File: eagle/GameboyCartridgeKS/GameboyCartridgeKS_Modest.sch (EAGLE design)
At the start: 20 parts, among them IC2 MEGA64-A, Y1 16MHz max

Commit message: Modest beta before wiring
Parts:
- added JOE: JUMPER-PAD-3-NOYES_SILK, SparkFun-Passives:JUMPER-PAD-3-NOYES_SILK
- added SCL, SCL1, SCL2, SCL3, SCL4, SDA: TEST-POINT3X5, SparkFun-Passives:TEST-POINT3X5
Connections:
- removed net 10: U$1.A4
- removed net 11: U$1.A5
- removed net 12: U$1.A6
- removed net 13: U$1.A7
- removed net 14: U$1.A8
- removed net 15: U$1.A9
- removed net 16: U$1.A10
- removed net 17: U$1.A11
- removed net 18: U$1.A12
- removed net 19: U$1.A13
- removed net 20: U$1.A14
- removed net 3: U$1./WR
- removed net 30: U$1./RS
- removed net 5: U$1./RCS
- removed net 6: U$1.A0
- removed net 7: U$1.A1
- removed net 8: U$1.A2
- removed net 9: U$1.A3
- new net !GB_CS: IC2.(XCK1)PD5, SCL4.1, U$1./RCS
- new net !GB_RD: IC2.(IC1)PD4, JOE.3, SCL3.1, U$1./RD
- new net !GB_RESET: IC2.(T1)PD6, U$1./RS
- new net !GB_WR: IC2.(TXD1/INT3)PD3, SCL2.1, U$1./WR
- new net GB_CLOCK: IC2.(RXD1/INT2)PD2, SCL1.1, U$1.NC
- new net GB_MIC_IN: IC2.(OC2/OC1C)PB7, U$1.VIN
- new net N$1: IC2.(SDA/INT1)PD1, SDA.1
- new net N$5: IC2.(SCL/INT0)PD0, SCL.1
- new net N$7: IC2.(OC0)PB4, JOE.1
- net !CE: now also IC2.(MISO)PB3; no longer U$1.A15
- net !OE: now also JOE.2; no longer U$1./RD
- net !RESET: now also IC2.(OC1B)PB6
- net !WE: now also IC2.(OC1A)PB5; no longer U$1.VIN
- net ADDRESS0: now also IC2.PF0(ADC0), U$1.A0; no longer IC2.(SCL/INT0)PD0
- net ADDRESS1: now also IC2.PF1(ADC1), U$1.A1; no longer IC2.(SDA/INT1)PD1
- net ADDRESS10: now also U$1.A10
- net ADDRESS11: now also U$1.A11
- net ADDRESS12: now also U$1.A12
- net ADDRESS13: now also U$1.A13
- net ADDRESS14: now also U$1.A14
- net ADDRESS15: now also U$1.A15
- net ADDRESS2: now also IC2.PF2(ADC2), U$1.A2; no longer IC2.(RXD1/INT2)PD2
- net ADDRESS3: now also IC2.PF3(ADC3), U$1.A3; no longer IC2.(TXD1/INT3)PD3
- net ADDRESS4: now also IC2.PF4(ADC4/TCK), U$1.A4; no longer IC2.(IC1)PD4
- net ADDRESS5: now also IC2.PF5(ADC5/TMS), U$1.A5; no longer IC2.(XCK1)PD5
- net ADDRESS6: now also IC2.PF6(ADC6/TDO), U$1.A6; no longer IC2.(T1)PD6
- net ADDRESS7: now also IC2.PF7(ADC7/TDI), U$1.A7; no longer IC2.(T2)PD7
- net ADDRESS8: now also U$1.A8
- net ADDRESS9: now also U$1.A9
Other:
- moved on the sheet: D1, JD1, PEN, TP1, TP2, TP3, TP4, TP5, TP6

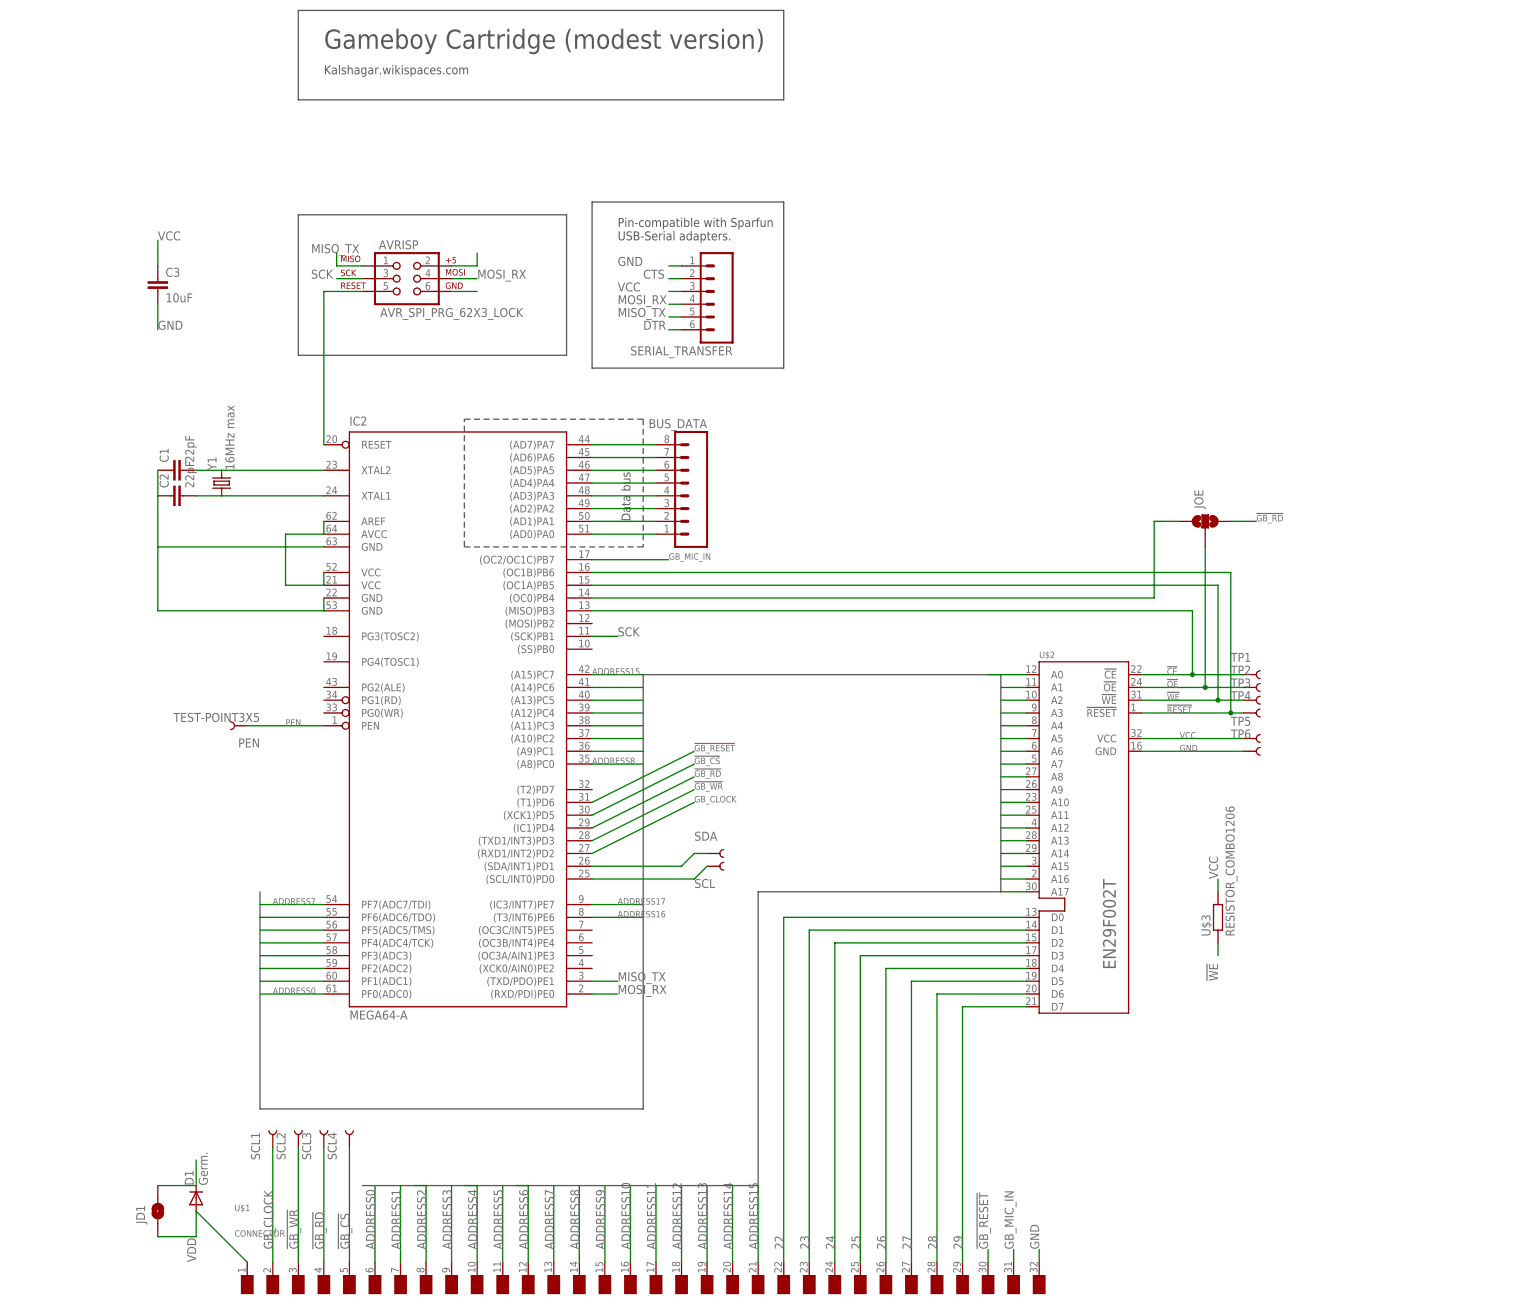
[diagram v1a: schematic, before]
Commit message: Schema finished, TODO start final placement.
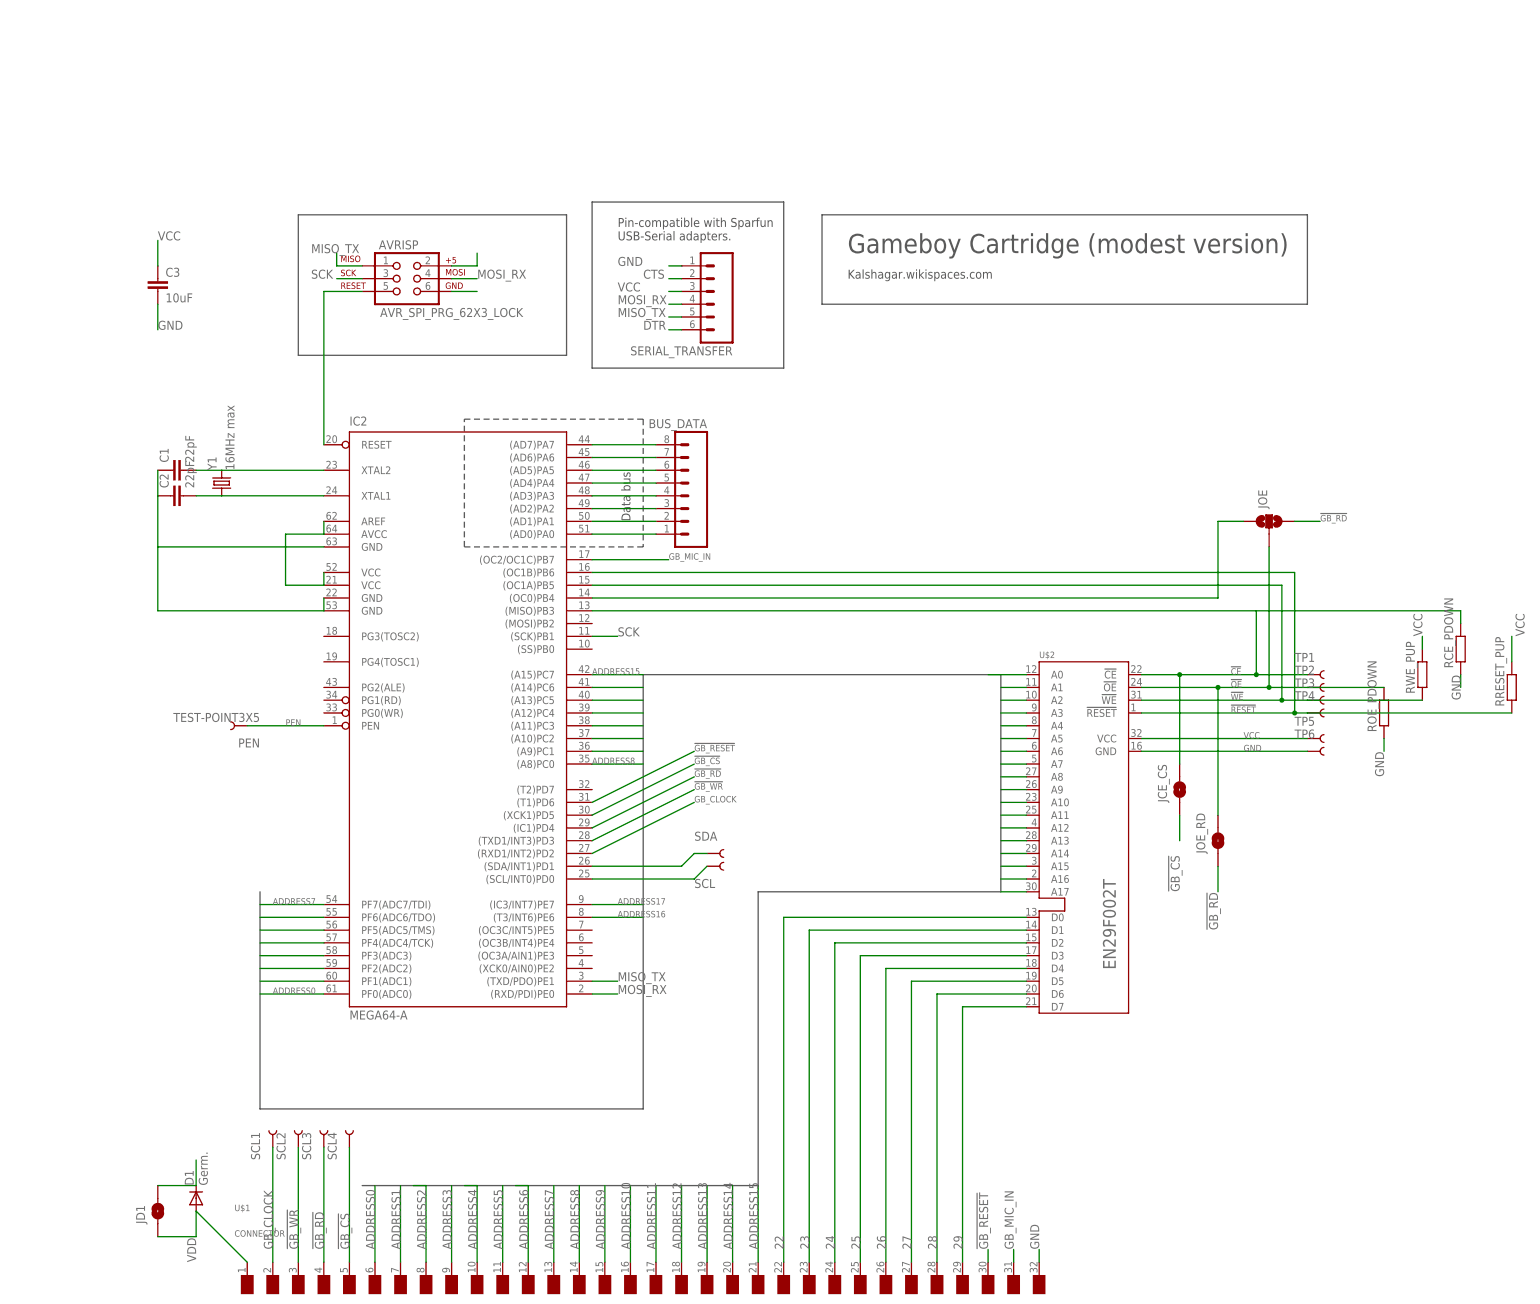
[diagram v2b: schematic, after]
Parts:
- removed U$3: RESISTOR_COMBO1206, kalshagar:RESISTOR_COMBO1206
- added JCE_CS, JOE_RD: JUMPER-PAD-2-NO, SparkFun-Passives:JUMPER-PAD-2-NO
- added RCE_PDOWN, ROE_PDOWN, RRESET_PUP, RWE_PUP: (no value), resistor:R-EU_R1206
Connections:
- net !CE: now also JCE_CS.2, RCE_PDOWN.2
- net !GB_CS: now also JCE_CS.1
- net !GB_RD: now also JOE_RD.1
- net !OE: now also JOE_RD.2, ROE_PDOWN.2
- net !RESET: now also RRESET_PUP.1
- net !WE: now also RWE_PUP.1; no longer U$3.1
- net GND: now also RCE_PDOWN.1, ROE_PDOWN.1
- net VCC: now also RRESET_PUP.2, RWE_PUP.2; no longer U$3.2
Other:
- moved on the sheet: JOE, TP1, TP2, TP3, TP4, TP5, TP6

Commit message: Placement beta before routing
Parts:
- added PEN1, PEN2, PEN3, PEN4: TEST-POINT3X5, SparkFun-Passives:TEST-POINT3X5
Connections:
- net GND: now also PEN1.1, PEN2.1
- net VCC: now also PEN3.1, PEN4.1
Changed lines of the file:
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@@
 <part name="JCE_CS" library="SparkFun-Passives" deviceset="JUMPER-PAD-2-NO" device="" value=""/>
 <part name="JOE_RD" library="SparkFun-Passives" deviceset="JUMPER-PAD-2-NO" device="" value=""/>
+<part name="PEN1" library="SparkFun-Passives" deviceset="TEST-POINT" device="3X5"/>
+<part name="PEN2" library="SparkFun-Passives" deviceset="TEST-POINT" device="3X5"/>
+<part name="PEN3" library="SparkFun-Passives" deviceset="TEST-POINT" device="3X5"/>
+<part name="PEN4" library="SparkFun-Passives" deviceset="TEST-POINT" device="3X5"/>
 </parts>
 <sheets>
@@
 <instance part="JCE_CS" gate="G$1" x="185.42" y="162.56" rot="R90"/>
 <instance part="JOE_RD" gate="G$1" x="193.04" y="152.4" rot="R90"/>
+<instance part="PEN1" gate="G$1" x="-27.94" y="256.54" rot="R180"/>
+<instance part="PEN2" gate="G$1" x="-27.94" y="251.46" rot="R180"/>
+<instance part="PEN3" gate="G$1" x="-27.94" y="271.78" rot="R180"/>
+<instance part="PEN4" gate="G$1" x="-27.94" y="269.24" rot="R180"/>
 </instances>
 <busses>
@@
 <wire x1="-17.78" y1="259.08" x2="-17.78" y2="254" width="0.1524" layer="91"/>
 <label x="-17.78" y="254" size="1.778" layer="95"/>
+<pinref part="PEN1" gate="G$1" pin="1"/>
+<wire x1="-17.78" y1="254" x2="-27.94" y2="254" width="0.1524" layer="91"/>
+<wire x1="-27.94" y1="254" x2="-27.94" y2="256.54" width="0.1524" layer="91"/>
+<pinref part="PEN2" gate="G$1" pin="1"/>
+<wire x1="-27.94" y1="256.54" x2="-27.94" y2="251.46" width="0.1524" layer="91"/>
 </segment>
 <segment>
@@
 <wire x1="-17.78" y1="266.7" x2="-17.78" y2="271.78" width="0.1524" layer="91"/>
 <label x="-17.78" y="271.78" size="1.778" layer="95"/>
-</segment>
-<segment>
+<pinref part="PEN3" gate="G$1" pin="1"/>
+<wire x1="-17.78" y1="271.78" x2="-27.94" y2="271.78" width="0.1524" layer="91"/>
+<pinref part="PEN4" gate="G$1" pin="1"/>
+<wire x1="-27.94" y1="271.78" x2="-27.94" y2="269.24" width="0.1524" layer="91"/>
+</segment>
+<segment>

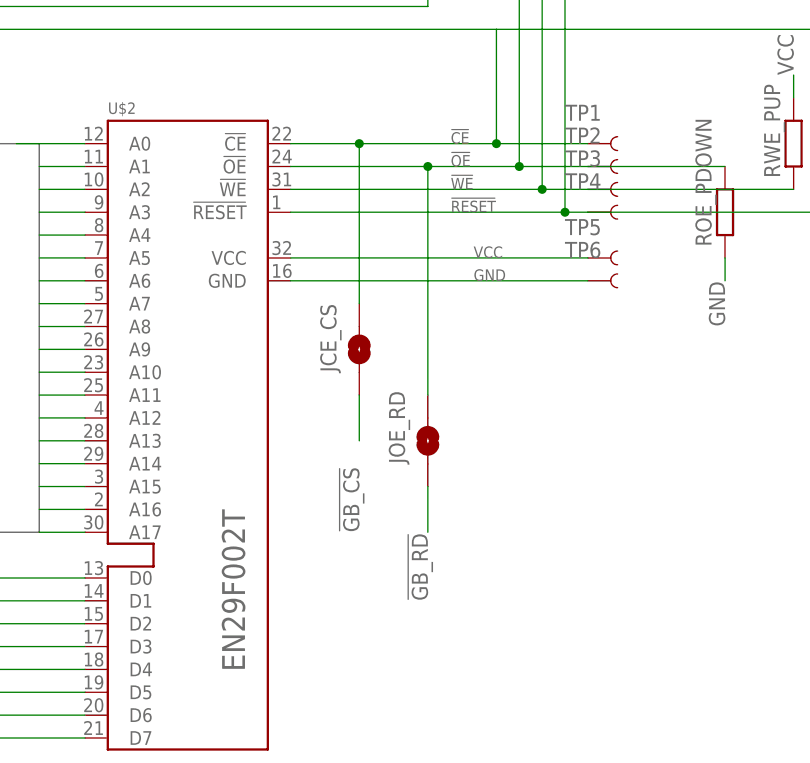
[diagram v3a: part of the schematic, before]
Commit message: Sent v1.0 MODEST to production
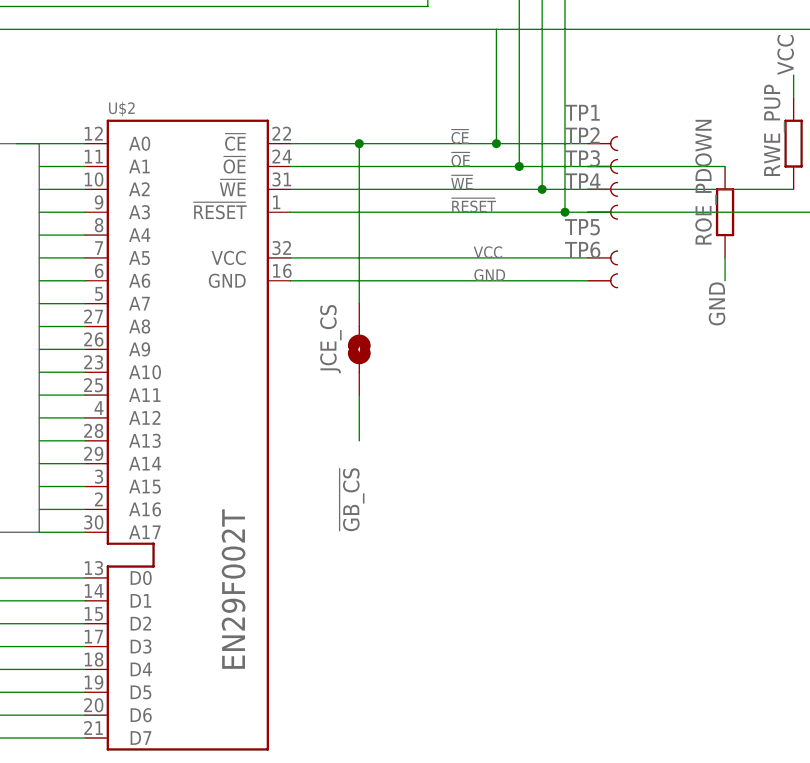
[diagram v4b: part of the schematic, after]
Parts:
- removed JOE_RD: JUMPER-PAD-2-NO, SparkFun-Passives:JUMPER-PAD-2-NO
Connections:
- net N$1 renamed SDA
- net N$5 renamed SCL
- net !GB_RD: no longer JOE_RD.1
- net !OE: no longer JOE_RD.2
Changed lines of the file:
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@@
 <part name="ROE_PDOWN" library="resistor" deviceset="R-EU_" device="R1206"/>
 <part name="JCE_CS" library="SparkFun-Passives" deviceset="JUMPER-PAD-2-NO" device="" value=""/>
-<part name="JOE_RD" library="SparkFun-Passives" deviceset="JUMPER-PAD-2-NO" device="" value=""/>
 <part name="PEN1" library="SparkFun-Passives" deviceset="TEST-POINT" device="3X5"/>
 <part name="PEN2" library="SparkFun-Passives" deviceset="TEST-POINT" device="3X5"/>
@@
 <instance part="ROE_PDOWN" gate="G$1" x="226.06" y="177.8" rot="R90"/>
 <instance part="JCE_CS" gate="G$1" x="185.42" y="162.56" rot="R90"/>
-<instance part="JOE_RD" gate="G$1" x="193.04" y="152.4" rot="R90"/>
 <instance part="PEN1" gate="G$1" x="-27.94" y="256.54" rot="R180"/>
 <instance part="PEN2" gate="G$1" x="-27.94" y="251.46" rot="R180"/>
@@
 <label x="213.36" y="215.9" size="1.27" layer="95"/>
 </segment>
-<segment>
-<pinref part="JOE_RD" gate="G$1" pin="1"/>
-<wire x1="193.04" y1="147.32" x2="193.04" y2="142.24" width="0.1524" layer="91"/>
-<label x="193.04" y="134.62" size="1.778" layer="95" rot="R90"/>
-</segment>
 </net>
 <net name="!WE" class="0">
@@
 </segment>
 </net>
-<net name="N$1" class="0">
+<net name="SDA" class="0">
 <segment>
 <pinref part="IC2" gate="G$1" pin="(SDA/INT1)PD1"/>
@@
 </segment>
 </net>
-<net name="N$5" class="0">
+<net name="SCL" class="0">
 <segment>
 <pinref part="IC2" gate="G$1" pin="(SCL/INT0)PD0"/>
@@
 <pinref part="U$2" gate="G$1" pin="!OE"/>
 <pinref part="TP2" gate="G$1" pin="1"/>
-<wire x1="177.8" y1="182.88" x2="193.04" y2="182.88" width="0.1524" layer="91"/>
+<wire x1="177.8" y1="182.88" x2="203.2" y2="182.88" width="0.1524" layer="91"/>
 <label x="195.58" y="182.88" size="1.27" layer="95"/>
 <pinref part="JOE" gate="G$1" pin="2"/>
-<wire x1="193.04" y1="182.88" x2="203.2" y2="182.88" width="0.1524" layer="91"/>
 <wire x1="203.2" y1="182.88" x2="210.82" y2="182.88" width="0.1524" layer="91"/>
 <wire x1="203.2" y1="210.82" x2="203.2" y2="182.88" width="0.1524" layer="91"/>
@@
 <pinref part="ROE_PDOWN" gate="G$1" pin="2"/>
 <wire x1="210.82" y1="182.88" x2="226.06" y2="182.88" width="0.1524" layer="91"/>
-<pinref part="JOE_RD" gate="G$1" pin="2"/>
-<wire x1="193.04" y1="182.88" x2="193.04" y2="157.48" width="0.1524" layer="91"/>
-<junction x="193.04" y="182.88"/>
-</segment>
-</net>
+</segment>
+</net>
